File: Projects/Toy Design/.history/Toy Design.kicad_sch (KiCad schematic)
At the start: 40 parts, among them J1 Conn_01x01_Pin, J2 Conn_01x01_Pin, J3 FTSH-107-01-X-DV-K-TR, U1 TLV61048DBVR, U10 STM32G030K6T6, U11 MCP3208-CI/SL, U2 MCP73123, U3 NCP1117-5.0_SOT223, U4 MLX90333, U5 A1330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

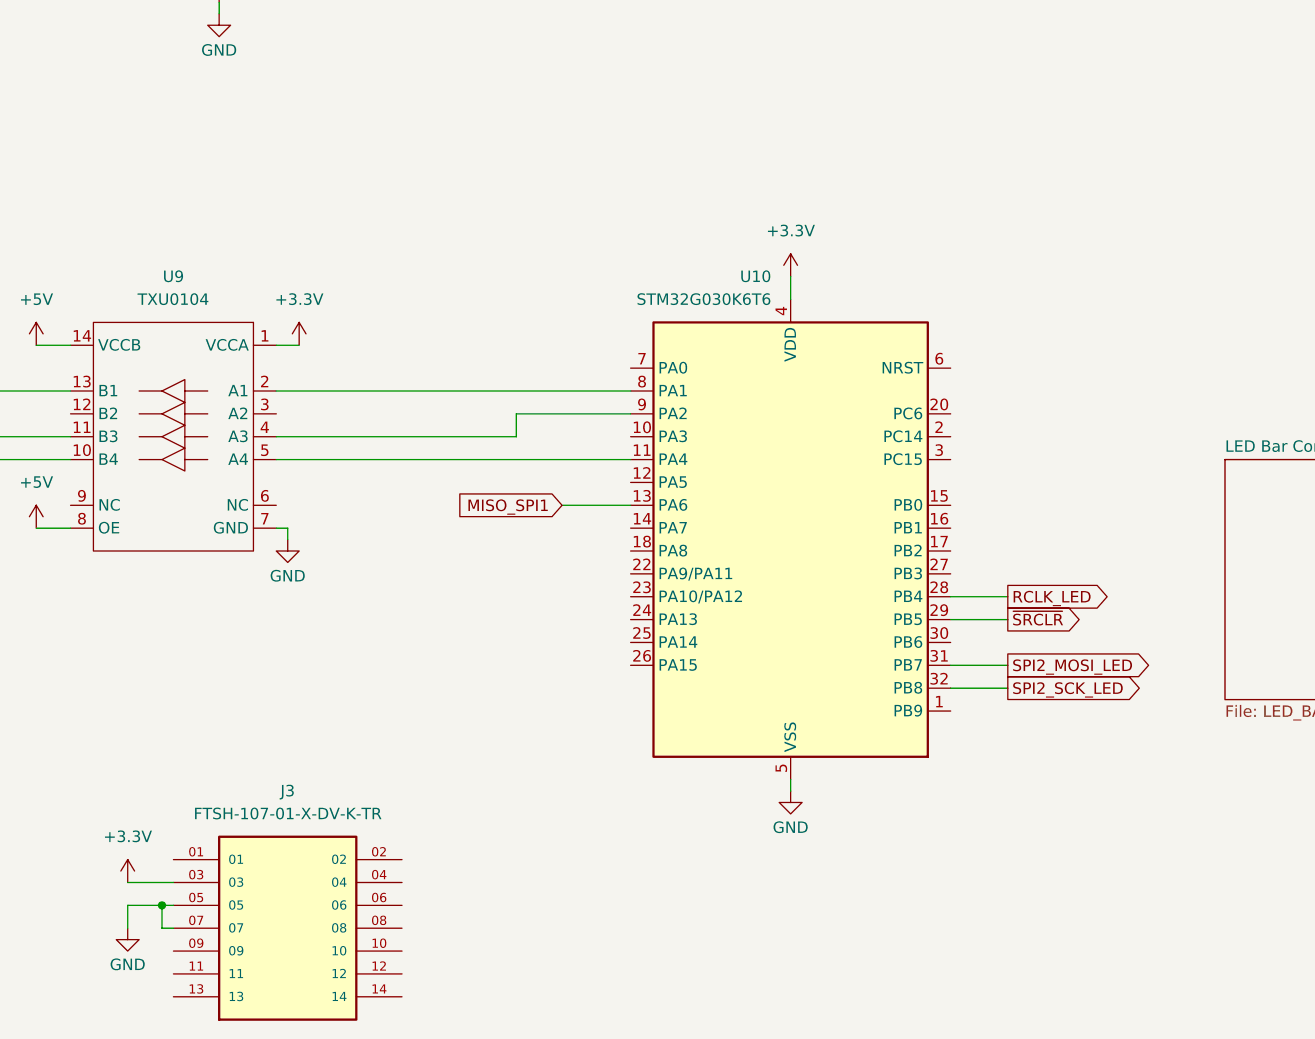
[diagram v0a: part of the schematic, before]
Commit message: Pushing connector connected to all signals
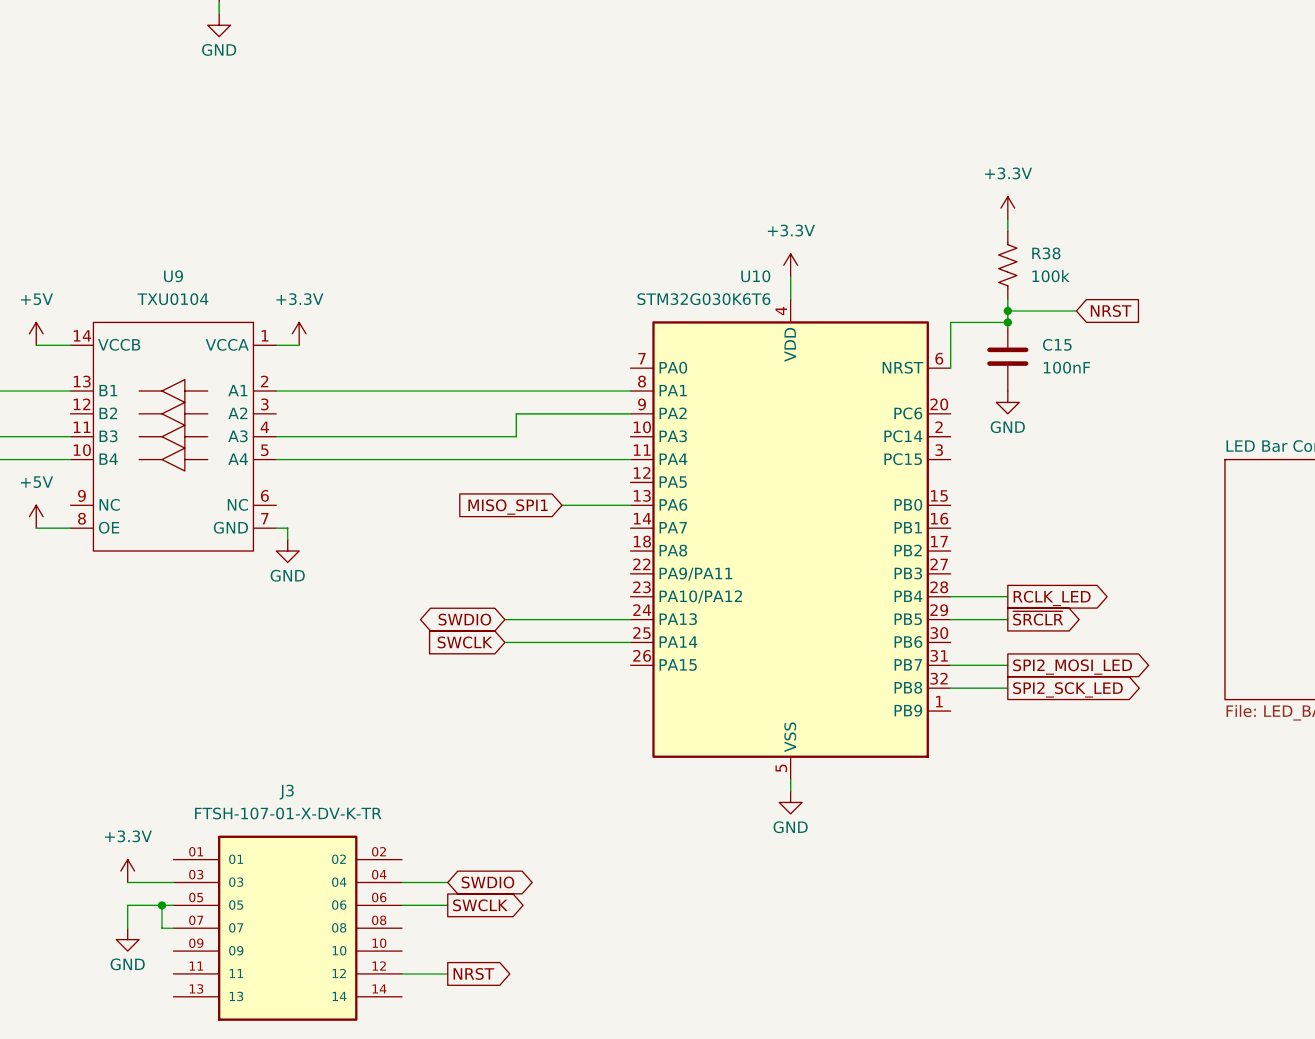
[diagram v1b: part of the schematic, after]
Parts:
- added C15: 100nF, Capacitor_SMD:C_0805_2012Metric_Pad1.18x1.45mm_HandSolder, symbol Toy_Design:C
- added R38: 100k, Resistor_SMD:R_0805_2012Metric_Pad1.20x1.40mm_HandSolder, symbol Device:R_US
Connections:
- net +3.3V: now also R38.1
- net GND: now also C15.2
- net SWDIO: now reaches J3.04
- net SWDIO: now also U10.24 (PA13)
- net SWCLK: now reaches J3.06
- net SWCLK: now also U10.25 (PA14)
- net NRST: now reaches J3.12
- net NRST: now also U10.6 (NRST), C15.1, R38.2

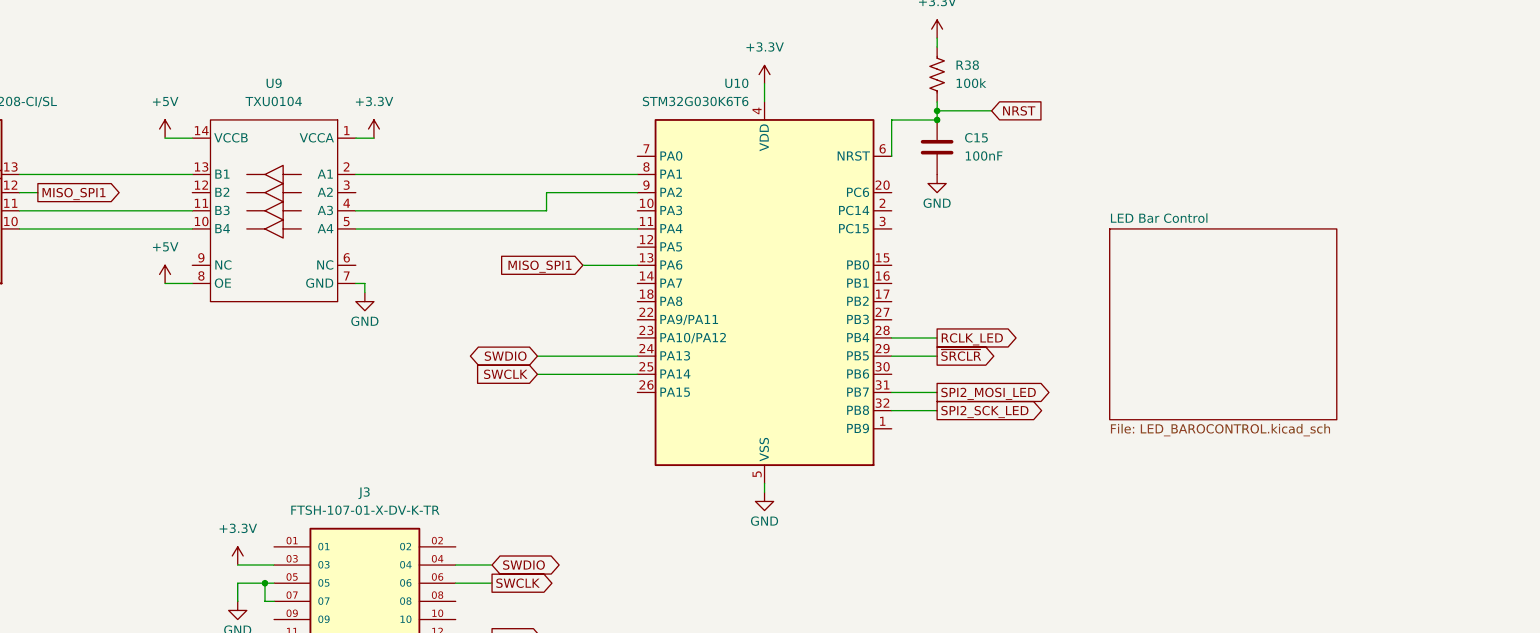
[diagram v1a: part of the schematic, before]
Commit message: Updated PCB edge to be inline with the design ifile in CLaude
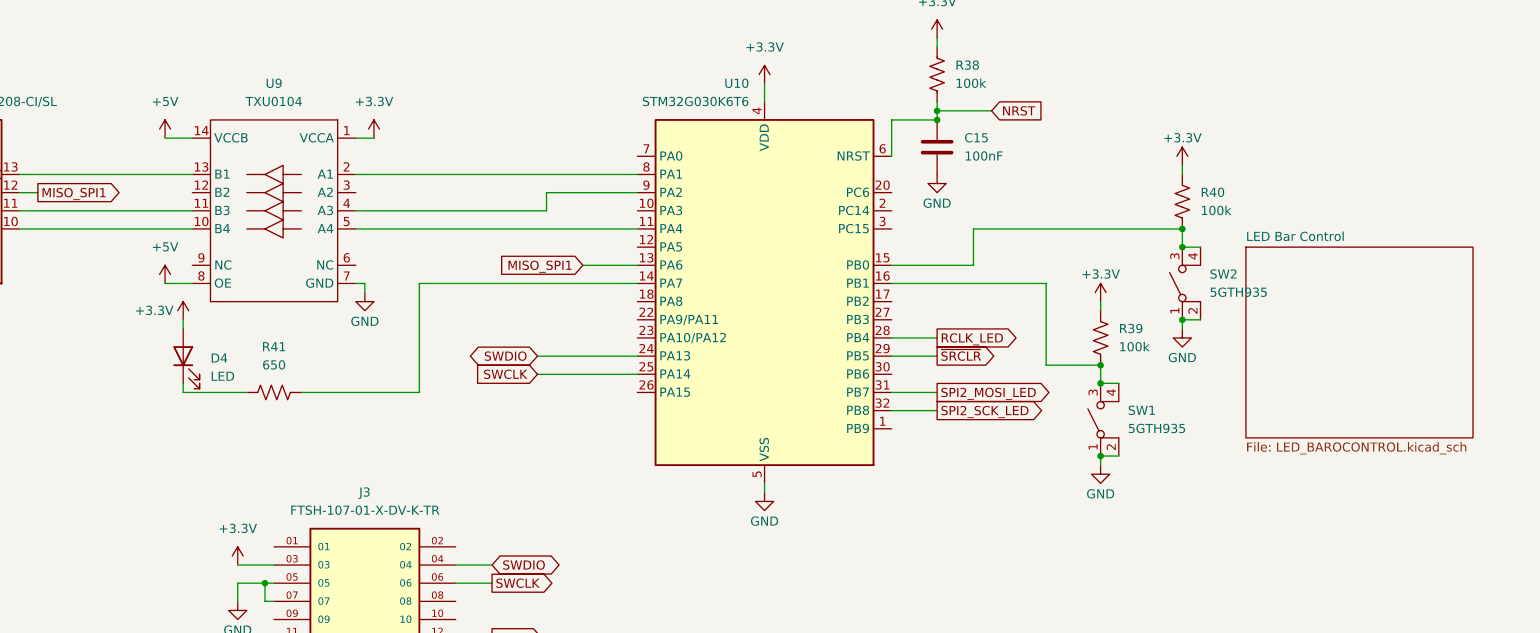
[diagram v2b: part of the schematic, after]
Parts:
- added D4: LED, LED_THT:LED_D5.0mm, symbol Device:LED
- added R39, R40: 100k, Resistor_SMD:R_0805_2012Metric_Pad1.20x1.40mm_HandSolder, symbol Device:R_US
- added R41: 650, Resistor_SMD:R_0805_2012Metric_Pad1.20x1.40mm_HandSolder, symbol Device:R_US
- added SW1, SW2: 5GTH935, ToyDesign:5GTH9, symbol Toy_Design:MEC_5G
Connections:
- net +3.3V: now also D4.2 (A), R39.1, R40.1
- net GND: now also SW1.1 (A), SW1.2 (B), SW2.1 (A), SW2.2 (B)
- net at U10.14 (PA7): now also R41.2
- net at U10.15 (PB0): now also R40.2, SW2.3 (A), SW2.4
- net at U10.16 (PB1): now also R39.2, SW1.3 (A), SW1.4
- new net: D4.1 (K), R41.1
